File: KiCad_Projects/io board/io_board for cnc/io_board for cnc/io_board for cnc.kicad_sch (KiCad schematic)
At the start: 6 parts, among them J1 Conn_01x05_Female, J2 Conn_01x02_Female, SW1 SW_DIP_x01, SW2 SW_DIP_x01, SW3 SW_DIP_x01, SW4 SW_DIP_x01

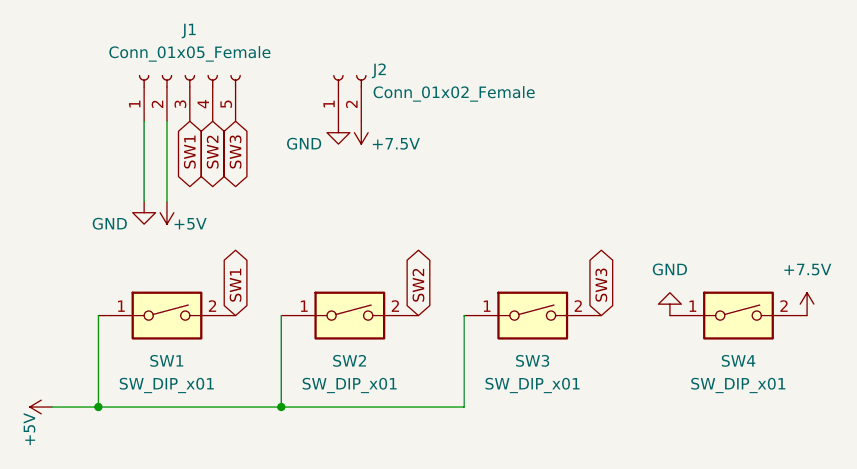
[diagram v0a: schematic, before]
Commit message: 部内大会用プログラムの作成
部内大会というか、北九州オープンくらいまでのプログラムが入ってます。
カメラ・IR_ring・Line_ringの制御。
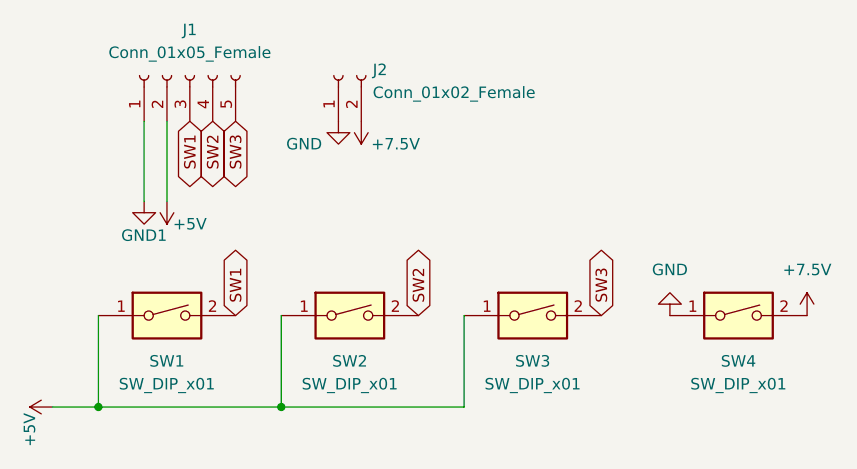
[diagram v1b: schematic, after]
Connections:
- net GND: no longer J1.1 (Pin_1)
- new net GND1: J1.1 (Pin_1)
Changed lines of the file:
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@@
     (pin "2")
+  )
+  (symbol (lib_id "power:GND1") (at 116.84 96.52 0) (unit 1)
+    (in_bom yes) (on_board yes)
+    (property "Reference" "#PWR02" (id 0) (at 116.84 102.87 0)
+      (effects (font (size 1.27 1.27)) hide)
+    )
+    (property "Value" "GND1" (id 1) (at 116.84 100.33 0))
+    (property "Footprint" "" (id 2) (at 116.84 96.52 0)
+      (effects (font (size 1.27 1.27)) hide)
+    )
+    (property "Datasheet" "" (id 3) (at 116.84 96.52 0)
+      (effects (font (size 1.27 1.27)) hide)
+    )
+    (pin "1")
   )
   (symbol (lib_id "power:+5V") (at 106.68 119.38 90) (unit 1)
@@
     )
     (property "Datasheet" "" (id 3) (at 140.97 87.63 0)
-      (effects (font (size 1.27 1.27)) hide)
-    )
-    (pin "1")
-  )
-  (symbol (lib_id "power:GND") (at 116.84 96.52 0) (unit 1)
-    (in_bom yes) (on_board yes)
-    (property "Reference" "#PWR02" (id 0) (at 116.84 102.87 0)
-      (effects (font (size 1.27 1.27)) hide)
-    )
-    (property "Value" "GND" (id 1) (at 113.03 99.06 0))
-    (property "Footprint" "" (id 2) (at 116.84 96.52 0)
-      (effects (font (size 1.27 1.27)) hide)
-    )
-    (property "Datasheet" "" (id 3) (at 116.84 96.52 0)
       (effects (font (size 1.27 1.27)) hide)
     )
@@
       (reference "#PWR01") (unit 1) (value "+5V") (footprint "")
     )
-    (path "/b409aa86-af44-407f-91ad-e545b77724b5"
-      (reference "#PWR02") (unit 1) (value "GND") (footprint "")
+    (path "/771cb5c1-62ba-4cca-999e-cdcbe417213c"
+      (reference "#PWR02") (unit 1) (value "GND1") (footprint "")
     )
     (path "/f061eaca-982f-4a4e-a231-de83aa44f7a4"
